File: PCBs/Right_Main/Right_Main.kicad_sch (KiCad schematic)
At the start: 13 parts, among them J10 Rotary switch pins 1, J5 Conn_IDC_Right_To_Left, J6 Screw terminal 5V GND Out, J7 Encoder inputs B, J8 Encoder inputs A, J9 Analog Inputs, U5 MCP23017_SP, U6 74HC4051, U7 ULN2003A

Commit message: wip
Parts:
- added J11, J4: Future expansion, symbol Connector_Generic:Conn_02x13_Odd_Even
- added J3: Conn_Right_Keypad, symbol System_Connectors:Conn_Right_Keypad
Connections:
- net +5V: now also J11.2 (Pin_2), J3.2 (5V), J4.2 (Pin_2)
- net GND: now also J5.1 (GND_1), J5.11 (GND_6), J5.13 (GND_7), J5.15 (GND_8), J5.17 (GND_9), J5.19 (GND_10), J5.21 (GND_11), J5.23 (GND_12), J5.25 (GND_13), J5.3 (GND_2), J5.5 (GND_3), J5.7 (GND_4), J5.9 (GND_5), J3.1 (GND_1), J3.3 (GND_2), J3.5 (GND_3), J3.7 (GND_4), J3.9 (GND_5), J4.1 (Pin_1), J4.11 (Pin_11), J4.13 (Pin_13), J4.15 (Pin_15), J4.17 (Pin_17), J4.19 (Pin_19), J4.21 (Pin_21), J4.23 (Pin_23), J4.25 (Pin_25), J4.3 (Pin_3), J4.5 (Pin_5), J4.7 (Pin_7), J4.9 (Pin_9)
- net Input register 1/CP: now also J11.8 (Pin_8), J3.8 (IN_CP)
- net Input register 1//PL: now also J11.10 (Pin_10), J3.10 (IN_PL)
- net Input register 4/DS: no longer J5.4 (IN_DSQ7)
- net at A1.D9, U6.10 (S1): now also J5.18 (ANA_S1), J11.20 (Pin_20)
- net at A1.D8, U6.11 (S0): now also J5.16 (ANA_S0), J11.18 (Pin_18)
- net at A1.D10, U6.9 (S2): now also J5.20 (ANA_S2), J11.22 (Pin_22)
- net at A1.A2: now also J4.12 (Pin_12)
- net at A1.A3: now also J4.10 (Pin_10)
- net at A1.A4: now also J4.8 (Pin_8)
- net at A1.A5: now also J11.26 (Pin_26)
- net at A1.D0 (D0/RX): now also J4.4 (Pin_4)
- net at A1.D1 (D1/TX): now also J4.6 (Pin_6)
- net at A1.D11, U7.1 (I1), U7.2 (I2)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: now also J5.22 (RSW_MD), J11.24 (Pin_24)
- net at A1.D12: now also J4.24 (Pin_24)
- net at A1.D13: now also J4.22 (Pin_22)
- net at A1.D2 (D2/SDA), J5.14 (I2C_SDA), U5.13 (SDA): now also J11.16 (Pin_16)
- net at A1.D3 (D3/SCL), J5.12 (I2C_SCL), U5.12 (SCK): now also J11.14 (Pin_14)
- net at A1.D7 (D7_INT4), J5.10 (IOX_INT), U5.20 (INTA): now also J11.12 (Pin_12)
- net at A1.MISO (SPI_MISO): now also J4.20 (Pin_20)
- net at A1.MOSI (SPI_MOSI): now also J4.18 (Pin_18)
- net at A1.SCK (SPI_SCK): now also J4.16 (Pin_16)
- net at A1.SS (SPI_CS): now also J4.14 (Pin_14)
- new net: J11.6 (Pin_6), J3.4 (IN_DFM)
- new net: J11.4 (Pin_4), J5.4 (IN_DTM)
- new net Input register 6/DS: J3.6 (IN_DTM)
- no-connect marks 5 -> 7
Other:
- added sheet Input register 5 (Input_Shift_Register.kicad_sch)
- added sheet Input register 6 (Input_Shift_Register.kicad_sch)
- moved on the sheet: C6, C7, J10, J5, J6, J7, J8, J9, U5, U6, U7

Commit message: wip
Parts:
- added R1, R2: 100, symbol Device:R_Small
- J9: value Analog Inputs -> Analog inputs
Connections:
- net Input register 1/CP: now also R1.2; no longer A1.D5
- net Input register 1//PL: now also R2.2; no longer A1.D6
- new net: A1.D6, R2.1
- new net: A1.D5, R1.1
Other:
- moved on the sheet: A1, C1, J6

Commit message: wip
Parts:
- added R3: 4.7k, symbol Device:R_Small
- added R4, R5: 15k, symbol Device:R_Small
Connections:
- net +5V: now also R3.1, R4.2, R5.2
- net at A1.D2 (D2/SDA), J11.16 (Pin_16), J5.14 (I2C_SDA)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: now also R5.1
- net at A1.D3 (D3/SCL), J11.14 (Pin_14), J5.12 (I2C_SCL)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: now also R4.1
- net at A1.D7 (D7_INT4), J11.12 (Pin_12), J5.10 (IOX_INT)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: now also R3.2

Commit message: wip
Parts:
- A1: footprint PCM_arduino-library:Arduino_Micro_Socket -> arduino-library:Arduino_Micro_Socket
- renumbered C6 to C1, C1 to C2, C7 to C3, J11 to J1, J6 to J2, J7 to J3, J8 to J4, J4 to J6, J3 to J7, J10 to J8, R5 to R1, R4 to R2, R1 to R4, R2 to R5, U5 to U1, U7 to U2, U6 to U3
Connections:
- net GND: now also J1.1 (Pin_1), J1.11 (Pin_11), J1.13 (Pin_13), J1.15 (Pin_15), J1.17 (Pin_17), J1.19 (Pin_19), J1.21 (Pin_21), J1.23 (Pin_23), J1.25 (Pin_25), J1.3 (Pin_3), J1.5 (Pin_5), J1.7 (Pin_7), J1.9 (Pin_9)
- no-connect marks 7 -> 8
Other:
- moved on the sheet: C2, J1, J2

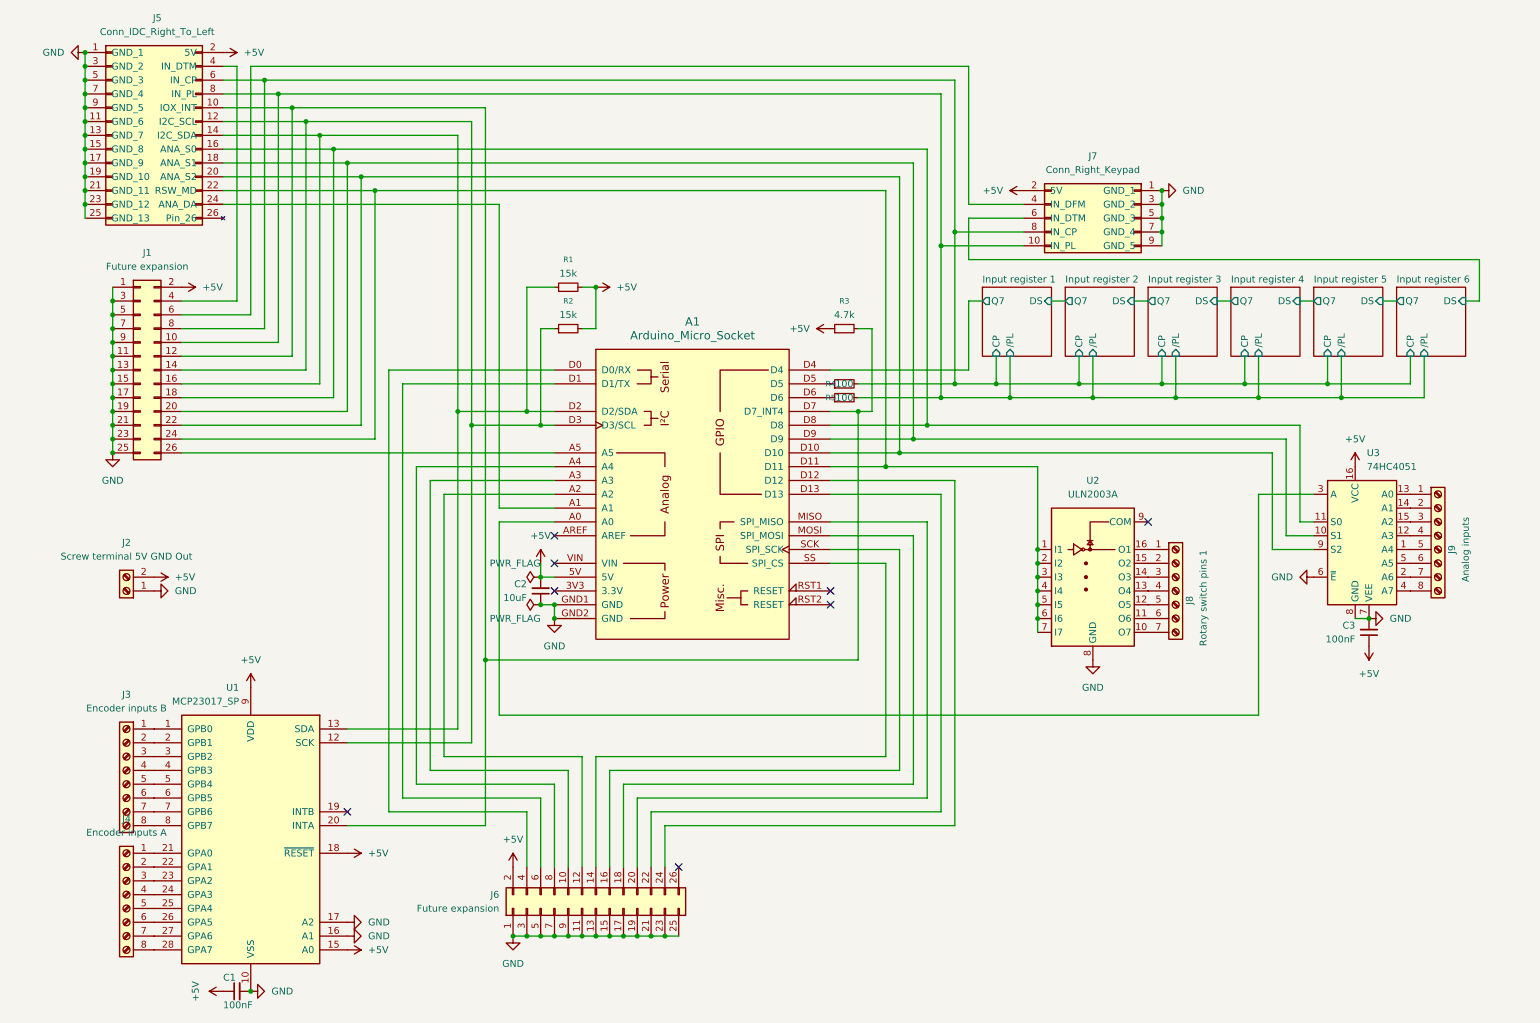
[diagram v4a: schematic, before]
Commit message: UART+RS485 + KiCad 10 + keypad PCB v1
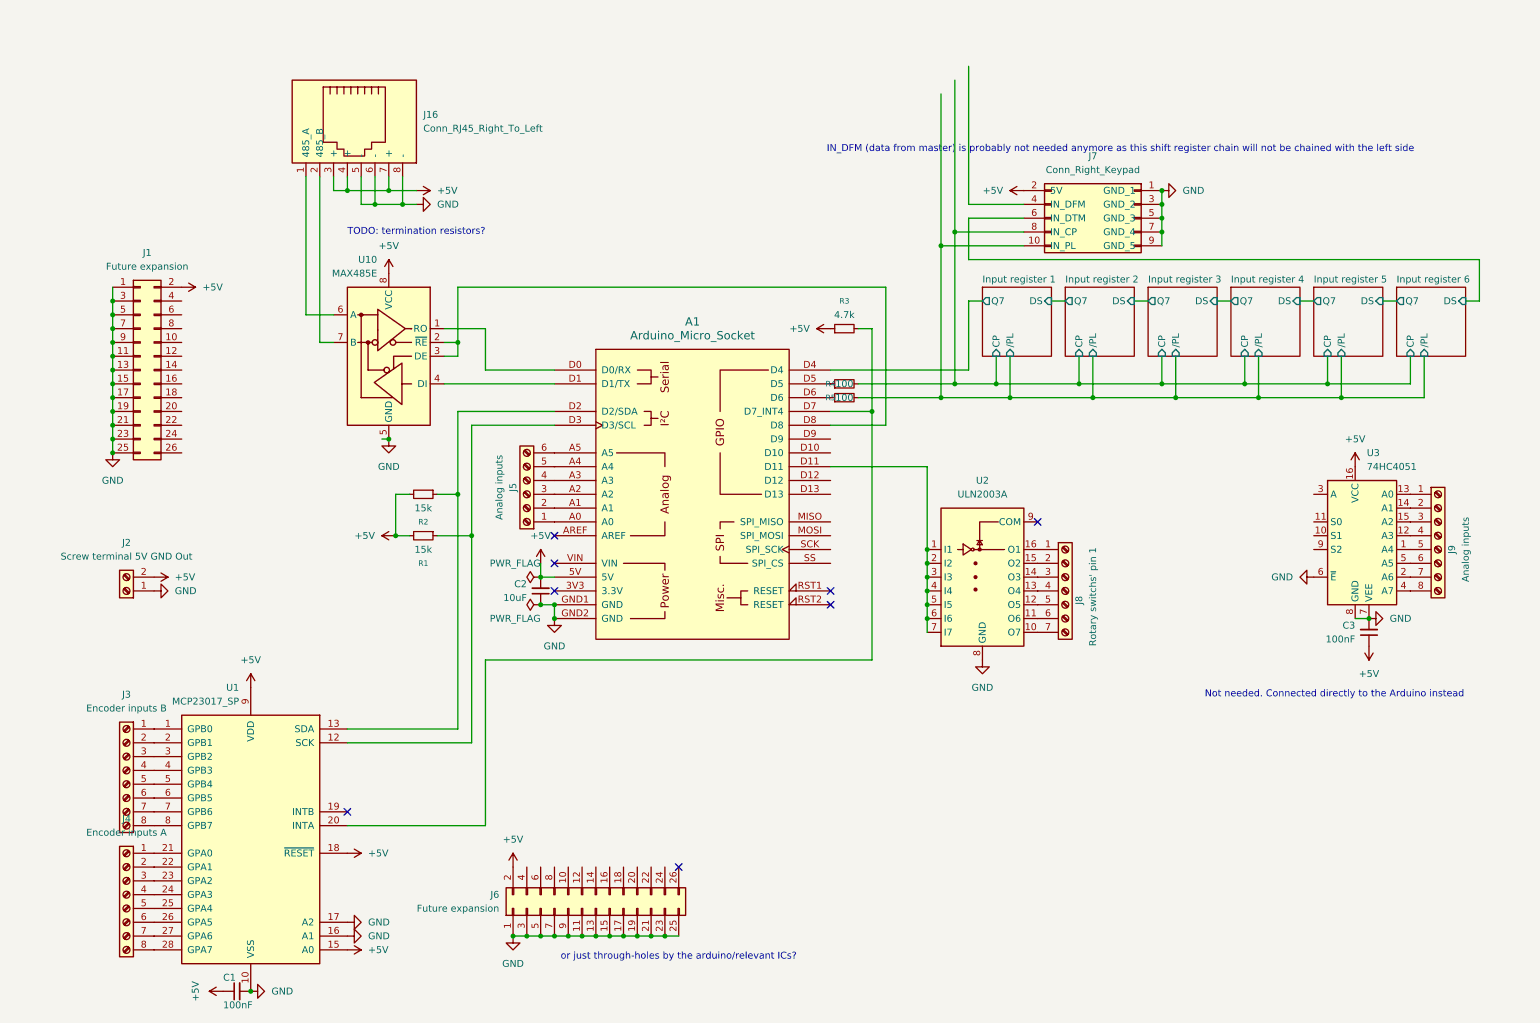
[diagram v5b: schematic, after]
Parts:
- removed J5: Conn_IDC_Right_To_Left, symbol System_Connectors:Conn_IDC_Right_To_Left
- added J16: Conn_RJ45_Right_To_Left, symbol System_Connectors:Conn_RJ45_Right_To_Left
- added J5: Analog inputs, symbol Connector:Screw_Terminal_01x06
- added U10: MAX485E, Package_SO:SOIC-8_3.9x4.9mm_P1.27mm, symbol Interface_UART:MAX485E
- J8: value Rotary switch pins 1 -> Rotary switchs' pin 1
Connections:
- net +5V: now also J16.3 (+), J16.4 (+), J16.7 (+), U10.8 (VCC)
- net GND: now also J16.5 (-), J16.6 (-), J16.8 (-), U10.5 (GND)
- net Input register 1/CP: no longer J1.8 (Pin_8)
- net Input register 1//PL: no longer J1.10 (Pin_10)
- net at U3.3 (A): no longer A1.A0
- net at J6.10 (Pin_10): no longer A1.A3
- net at J6.12 (Pin_12): no longer A1.A2
- net at J6.14 (Pin_14): no longer A1.SS (SPI_CS)
- net at J6.16 (Pin_16): no longer A1.SCK (SPI_SCK)
- net at J6.18 (Pin_18): no longer A1.MOSI (SPI_MOSI)
- net at J6.20 (Pin_20): no longer A1.MISO (SPI_MISO)
- net at J6.22 (Pin_22): no longer A1.D13
- net at J6.24 (Pin_24): no longer A1.D12
- net at J6.4 (Pin_4): no longer A1.D0 (D0/RX)
- net at J6.6 (Pin_6): no longer A1.D1 (D1/TX)
- net at J6.8 (Pin_8): no longer A1.A4
- net at J7.4 (IN_DFM): no longer J1.6 (Pin_6)
- net at A1.D2 (D2/SDA), U1.13 (SDA): now also R2.1; no longer J1.16 (Pin_16), R1.1
- net at A1.A1: now also J5.2 (Pin_2)
- net at A1.A5: now also J5.6 (Pin_6); no longer J1.26 (Pin_26)
- net at A1.D11, U2.1 (I1), U2.2 (I2)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: no longer J1.24 (Pin_24)
- net at A1.D3 (D3/SCL), U1.12 (SCK): now also R1.1; no longer J1.14 (Pin_14), R2.1
- net at A1.D7 (D7_INT4), R3.2, U1.20 (INTA): no longer J1.12 (Pin_12)
- new net: A1.A0, J5.1 (Pin_1)
- new net: A1.A2, J5.3 (Pin_3)
- new net: A1.A3, J5.4 (Pin_4)
- new net: A1.A4, J5.5 (Pin_5)
- new net: A1.D0 (D0/RX), U10.1 (RO)
- new net: A1.D1 (D1/TX), U10.4 (DI)
- new net: A1.D8, U10.2 (~{RE}), U10.3 (DE)
- new net: J16.1 (485_A), U10.6 (A)
- new net: J16.2 (485_B), U10.7 (B)
- now unconnected: A1.D10, A1.D9, J1.18 (Pin_18), J1.20 (Pin_20), J1.22 (Pin_22), U3.10 (S1), U3.11 (S0), U3.9 (S2)
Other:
- note added: "IN_DFM (data from master) is probably not needed anymore as this shift register chain will not be chained with the left side"
- note added: "Not needed. Connected directly to the Arduino instead"
- note added: "TODO: termination resistors?"
- note added: "or just through-holes by the arduino/relevant ICs?"
- moved on the sheet: J8, R1, R2, U2
